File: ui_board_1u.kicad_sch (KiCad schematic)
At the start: 39 parts, among them J1 X9555WV-2x06-6TV01, U1 AFC01-S30FCA-00, U2 SPX3819M5-L, U3 TPS61040DBV

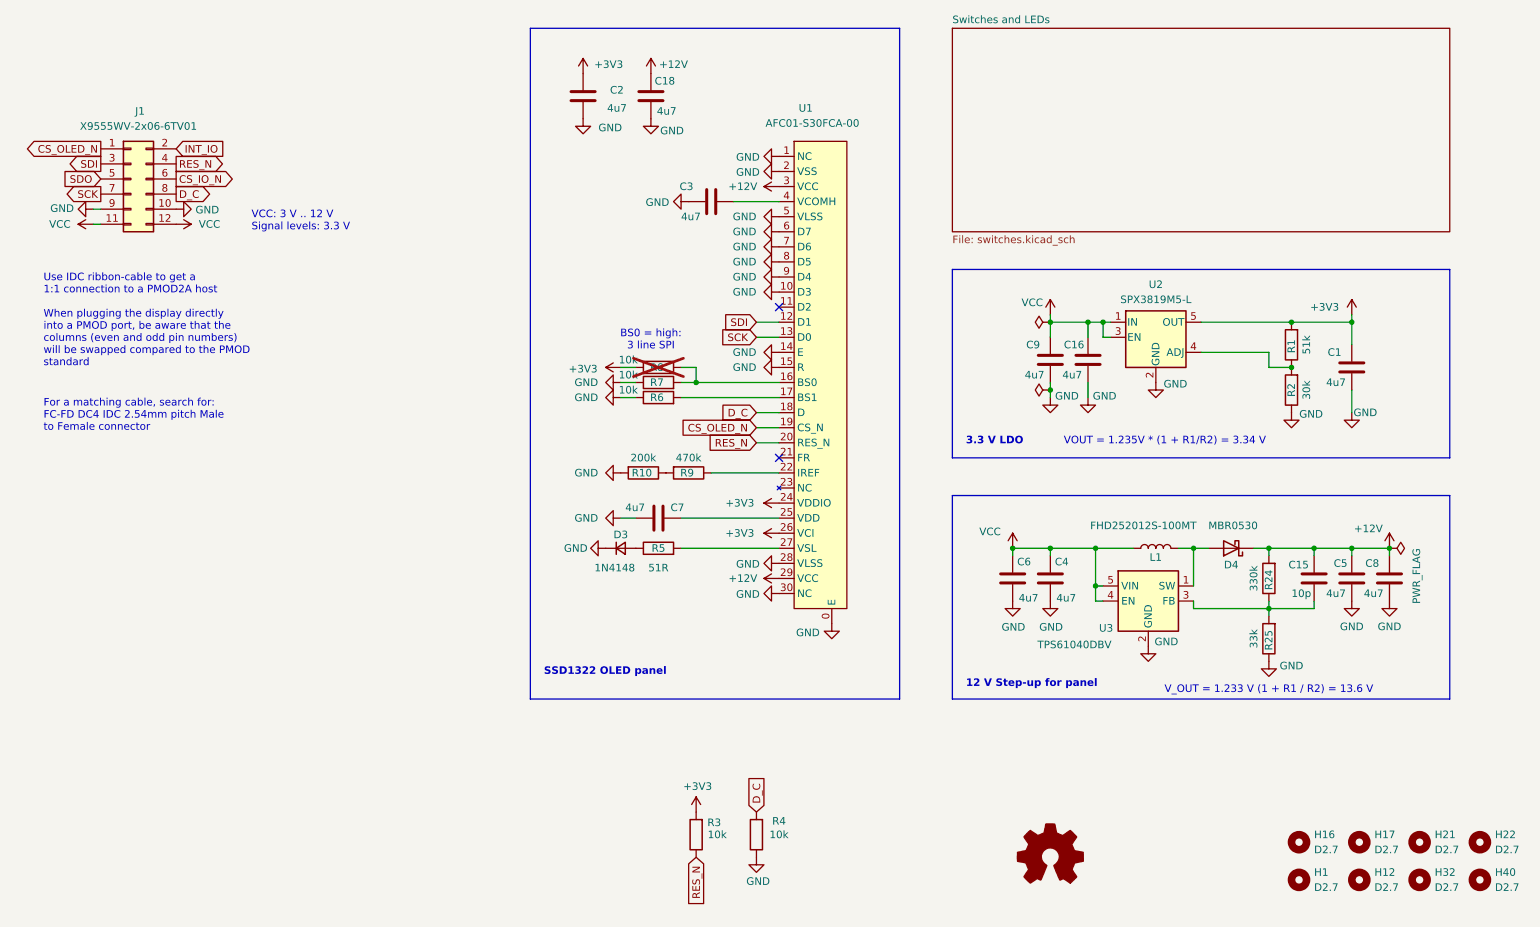
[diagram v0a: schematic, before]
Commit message: switch to 4 layers, rough routing done
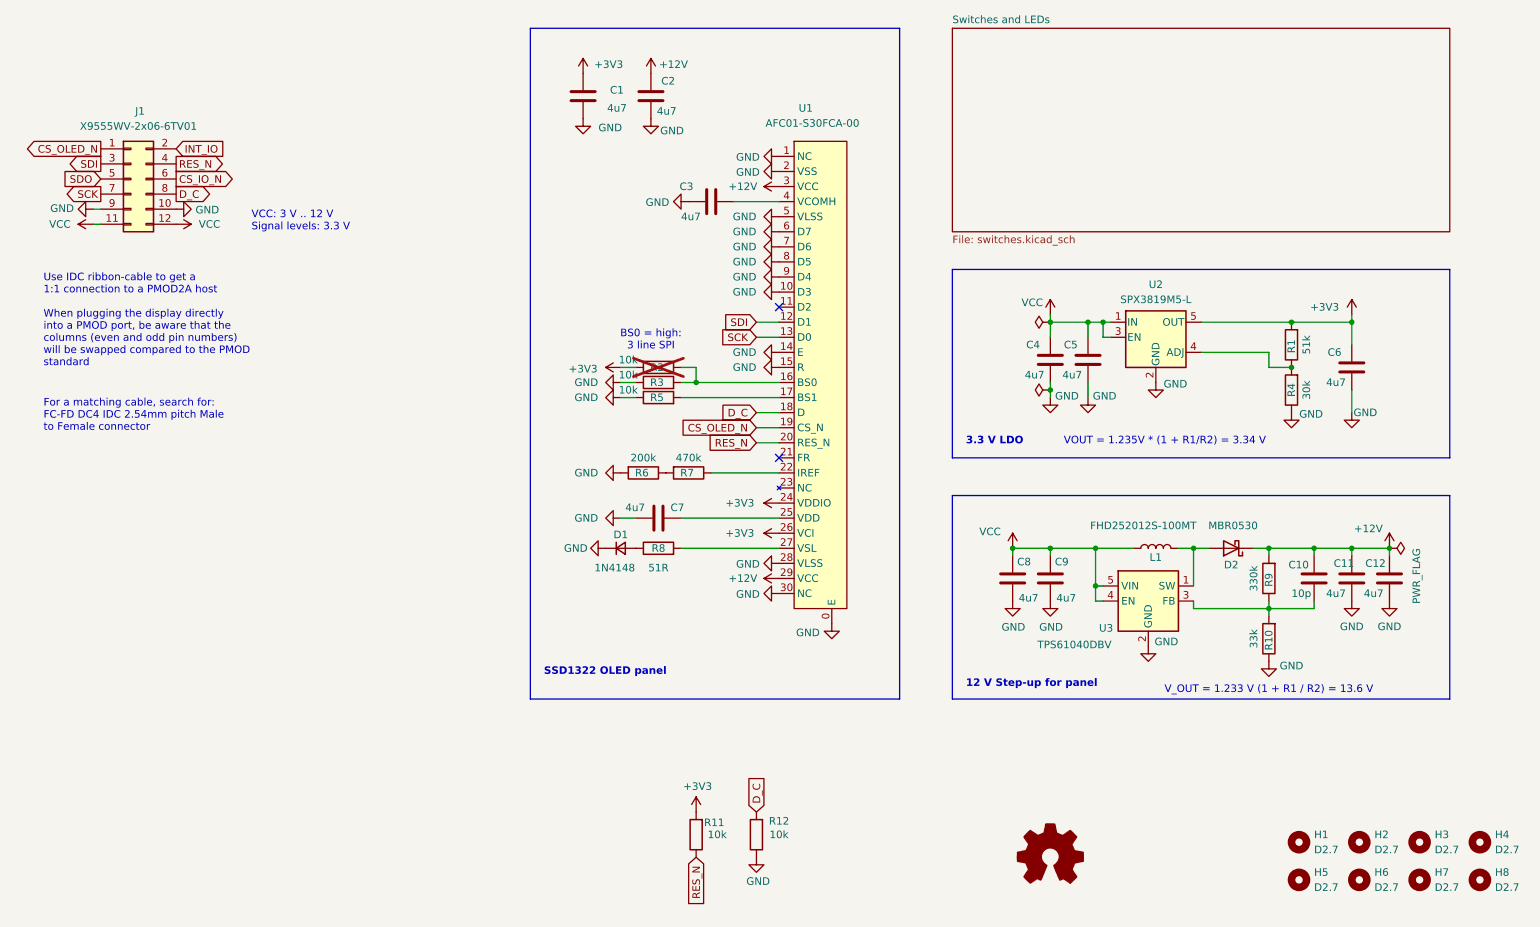
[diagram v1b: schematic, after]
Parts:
- renumbered C2 to C1, C15 to C10, C5 to C11, C8 to C12, C18 to C2, C9 to C4, C16 to C5, C1 to C6, C6 to C8, C4 to C9, D3 to D1, D4 to D2, H16 to H1, H17 to H2, H21 to H3, H22 to H4, H1 to H5, H12 to H6, H32 to H7, H40 to H8, R25 to R10, R3 to R11, R4 to R12, R8 to R2, R7 to R3, R2 to R4, R6 to R5, R10 to R6, R9 to R7, R5 to R8, R24 to R9
